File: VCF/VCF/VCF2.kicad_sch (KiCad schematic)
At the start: 32 parts, among them J13 Conn_02x05_Odd_Even, J2 Conn_01x08, J3 Conn_01x08, U5 TL072, U6 LM13700

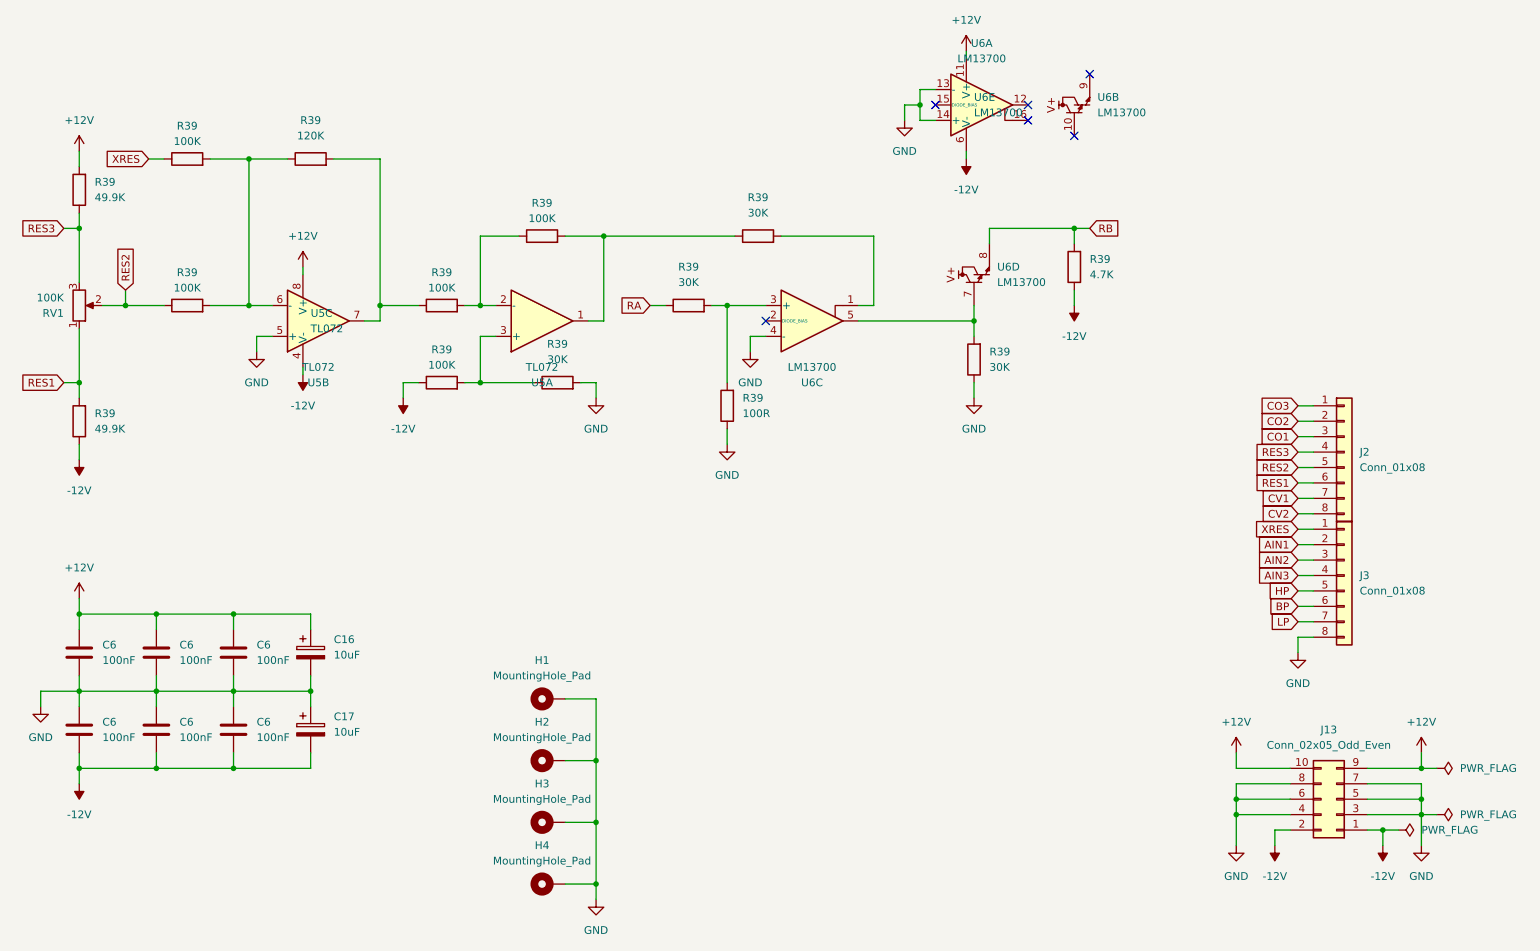
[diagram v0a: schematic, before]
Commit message: VCF - fully routed
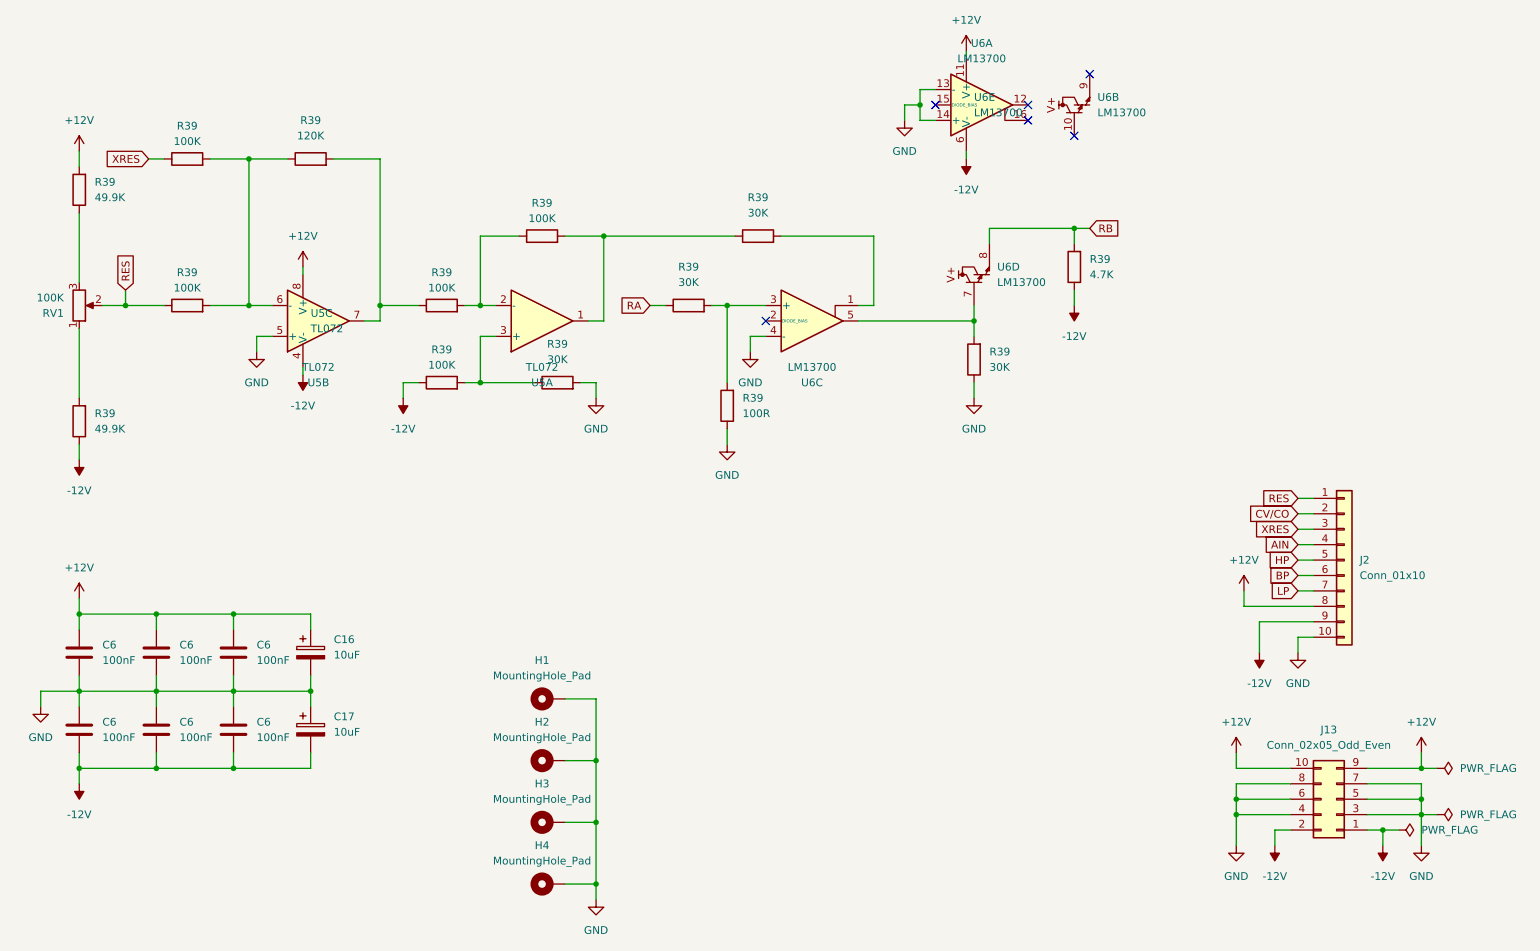
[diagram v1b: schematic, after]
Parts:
- removed J2, J3: Conn_01x08, Connector_PinHeader_2.54mm:PinHeader_1x08_P2.54mm_Vertical, symbol Connector_Generic:Conn_01x08
- added J2: Conn_01x10, Connector_PinHeader_2.54mm:PinHeader_1x10_P2.54mm_Vertical, symbol Connector_Generic:Conn_01x10
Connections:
- net +12V: now also J2.8 (Pin_8)
- net -12V: now also J2.9 (Pin_9)
- net BP: now also J2.6 (Pin_6)
- net GND: now also J2.10 (Pin_10)
- net HP: now also J2.5 (Pin_5)
- net LP: now also J2.7 (Pin_7)
- net XRES: now also J2.3 (Pin_3)
- net RES1: no longer names the net of R39.2, RV1.1
- net RES2 renamed RES
- net RES: now also J2.1 (Pin_1)
- net RES3: no longer names the net of R39.1, RV1.3
- new net AIN: J2.4 (Pin_4)
- new net CV/CO: J2.2 (Pin_2)

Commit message: VCF - fix some components value
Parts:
- H1, H2, H3, H4: now left out of the parts list
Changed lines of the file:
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@@
   )
   (symbol (lib_id "Mechanical:MountingHole_Pad") (at 115.57 148.59 90) (unit 1)
-    (in_bom yes) (on_board yes) (dnp no) (fields_autoplaced)
+    (in_bom no) (on_board yes) (dnp no) (fields_autoplaced)
     (property "Reference" "H3" (at 114.3 142.24 90)
       (effects (font (size 1.27 1.27)))
@@
   )
   (symbol (lib_id "Mechanical:MountingHole_Pad") (at 115.57 158.75 90) (unit 1)
-    (in_bom yes) (on_board yes) (dnp no) (fields_autoplaced)
+    (in_bom no) (on_board yes) (dnp no) (fields_autoplaced)
     (property "Reference" "H4" (at 114.3 152.4 90)
       (effects (font (size 1.27 1.27)))
@@
   )
   (symbol (lib_id "Mechanical:MountingHole_Pad") (at 115.57 128.27 90) (unit 1)
-    (in_bom yes) (on_board yes) (dnp no) (fields_autoplaced)
+    (in_bom no) (on_board yes) (dnp no) (fields_autoplaced)
     (property "Reference" "H1" (at 114.3 121.92 90)
       (effects (font (size 1.27 1.27)))
@@
   )
   (symbol (lib_id "Mechanical:MountingHole_Pad") (at 115.57 138.43 90) (unit 1)
-    (in_bom yes) (on_board yes) (dnp no) (fields_autoplaced)
+    (in_bom no) (on_board yes) (dnp no) (fields_autoplaced)
     (property "Reference" "H2" (at 114.3 132.08 90)
       (effects (font (size 1.27 1.27)))
